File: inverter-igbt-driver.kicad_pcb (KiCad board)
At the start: 2 copper layers, 84.5 x 64 mm, 68 parts, among them J1 Conn_01x09, U1 NE555, U2 IXDF604SIA, U3 FOD8316, U5 FOD8316, U6 Transformer_2P_2S, U8 Transformer_2P_2S, U9 IGBT_HALF_BRIDGE

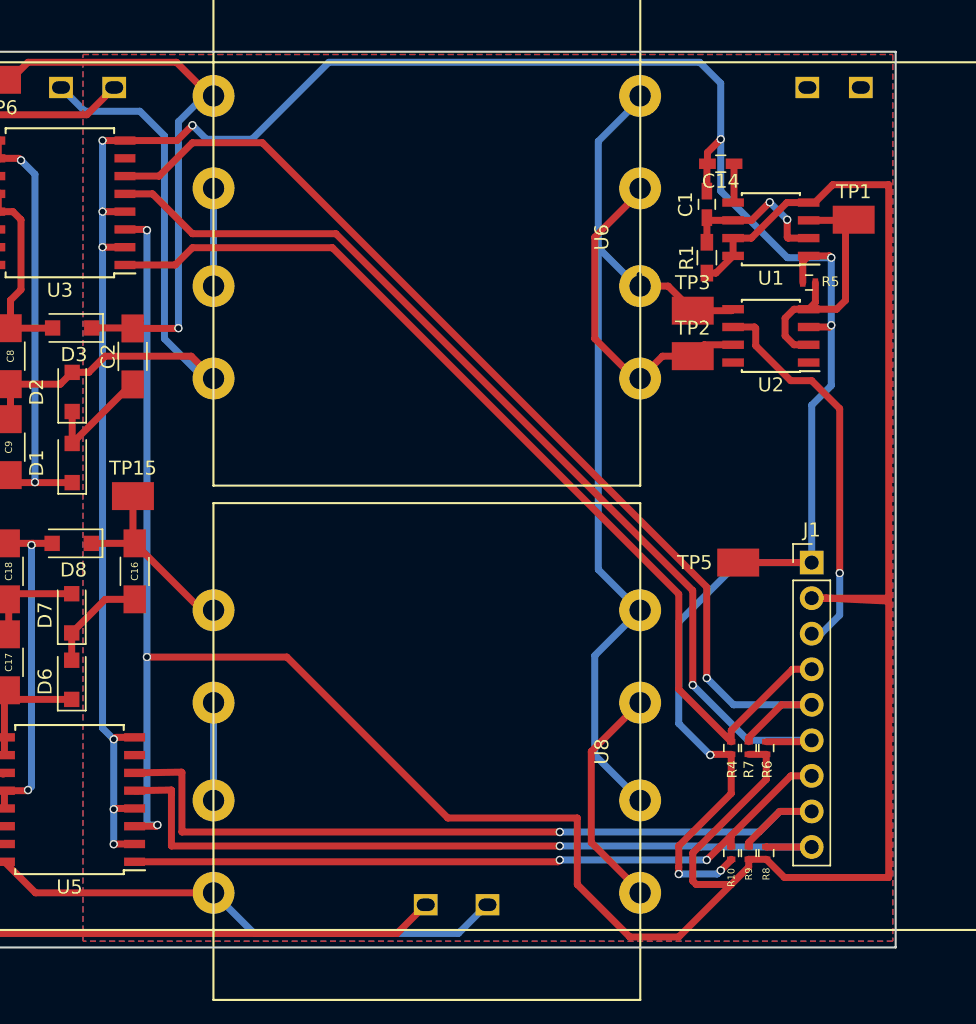
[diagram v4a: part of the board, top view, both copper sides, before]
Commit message: Adds NTC to connector.
Completes 555 rewire.

Rewires IGBT signals to layout more simply.
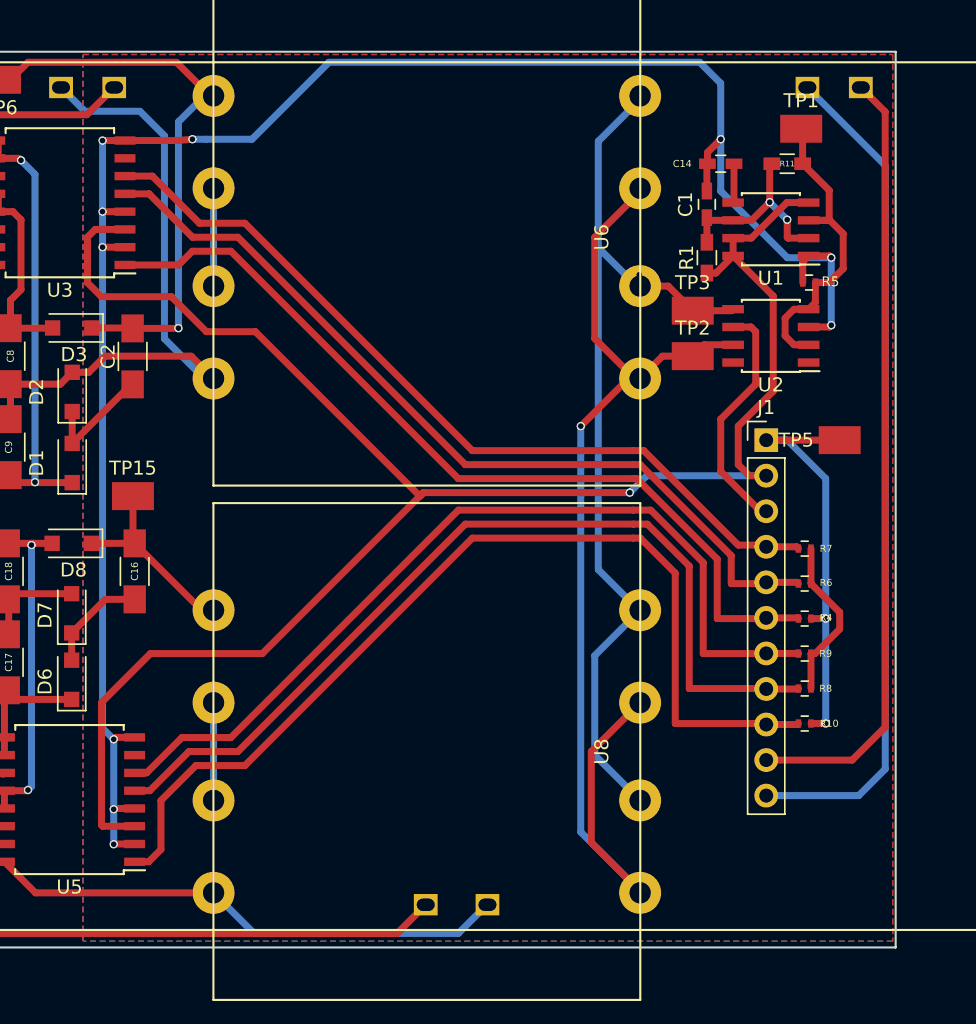
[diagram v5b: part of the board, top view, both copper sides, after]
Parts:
- added R11: 1.5k, Resistors_SMD:R_0603_HandSoldering, F.Cu at (169.8, 29.0)
- J1: value Conn_01x09 -> CONTROL; footprint Pin_Headers:Pin_Header_Straight_1x09_Pitch2.54mm -> Pin_Headers:Pin_Header_Straight_1x11_Pitch2.54mm
- moved R7 14.8 mm to (171.0, 56.5), turned to 180 degrees
- moved R9 14.8 mm to (171.0, 64.0), turned to 180 degrees
- moved R6 12.1 mm to (171.0, 59.0), turned to 180 degrees
- moved R8 12.1 mm to (171.0, 66.5), turned to 180 degrees
- moved TP5 11.4 mm to (173.5, 48.8)
- moved R10 10.6 mm to (171.0, 69.0), turned to 0 degrees
- moved R4 10.6 mm to (171.0, 61.5), turned to 0 degrees
- moved J1 9.33 mm to (168.2, 48.8)
- moved TP1 7.50 mm to (170.8, 26.5)
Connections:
- J1 pad 4: /VIN_H -> /FAULT_H
- J1 pad 5: /FAULT_H -> /RESET_H
- J1 pad 6: /RESET_H -> /VIN_H
- J1 pad 7: /VIN_L -> /FAULT_L
- J1 pad 8: /FAULT_L -> /RESET_L
- J1 pad 9: /RESET_L -> /VIN_L
- U9 pad 5: Net-(U9-Pad5) -> /NTC+
- U9 pad 6: Net-(U9-Pad6) -> /NTC-
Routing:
- net +5V: track 205.7 -> 143.8 mm, vias 3 -> 1
- net /NTC-: track 0.00 -> 60.3 mm
- net /NTC+: track 0.00 -> 55.9 mm
- net /negative/SQUARE_H: track 40.5 -> 81.2 mm, vias 0 -> 1
- net GND: track 198.6 -> 167.6 mm, vias 13 -> 12
- net /VIN_L: track 51.7 -> 70.9 mm, vias 2 -> 0
- net /FAULT_H: track 76.3 -> 59.1 mm, vias 1 -> 0
- net /RESET_H: track 72.5 -> 60.9 mm, vias 1 -> 0
- net +24V: track 28.1 -> 17.2 mm, vias 1 -> 0
- net /RESET_L: track 55.7 -> 65.3 mm, vias 1 -> 0
- net /VIN_H: track 70.8 -> 61.9 mm
- net Net-(R11-Pad1): track 18.1 -> 23.8 mm
- net /FAULT_L: track 59.0 -> 63.3 mm, vias 1 -> 0
- net Net-(C1-Pad1): track 11.4 -> 14.3 mm

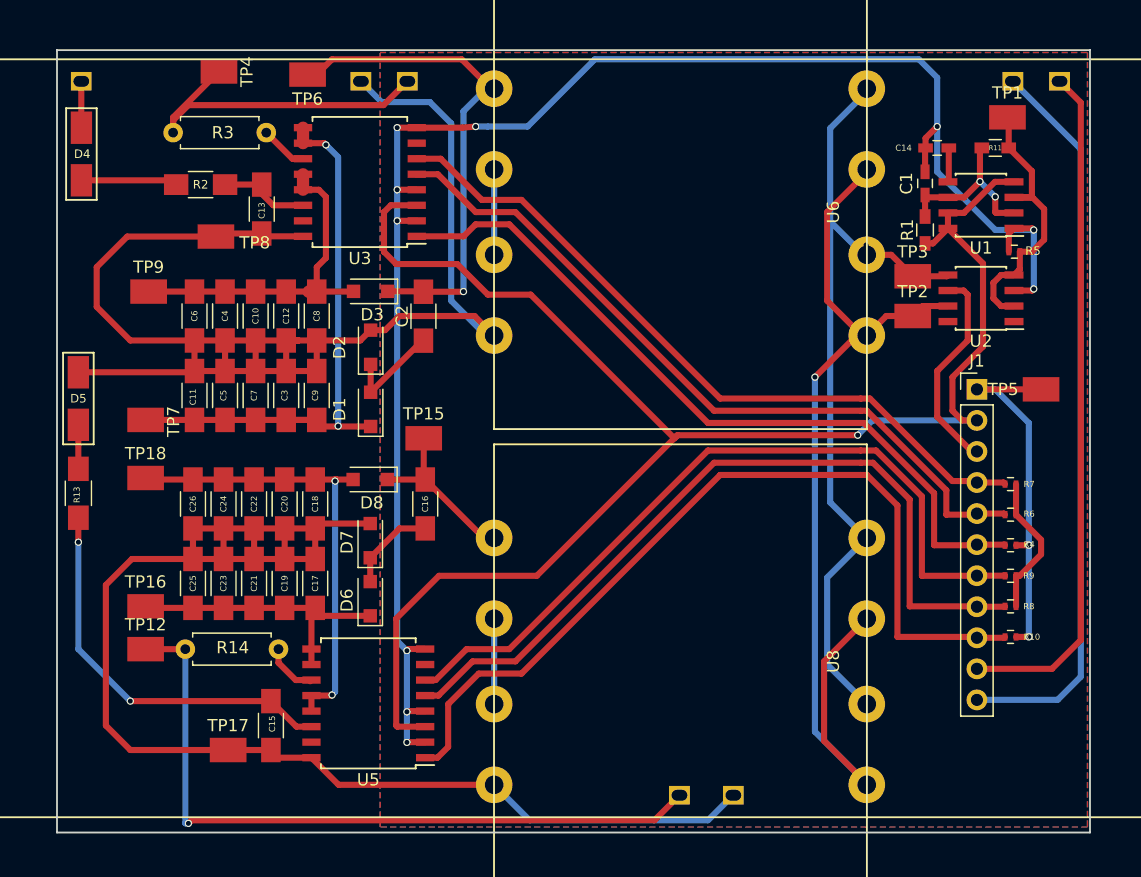
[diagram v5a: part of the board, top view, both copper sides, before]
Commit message: Fix hole size for avoiding slotting in OshPark drilling.
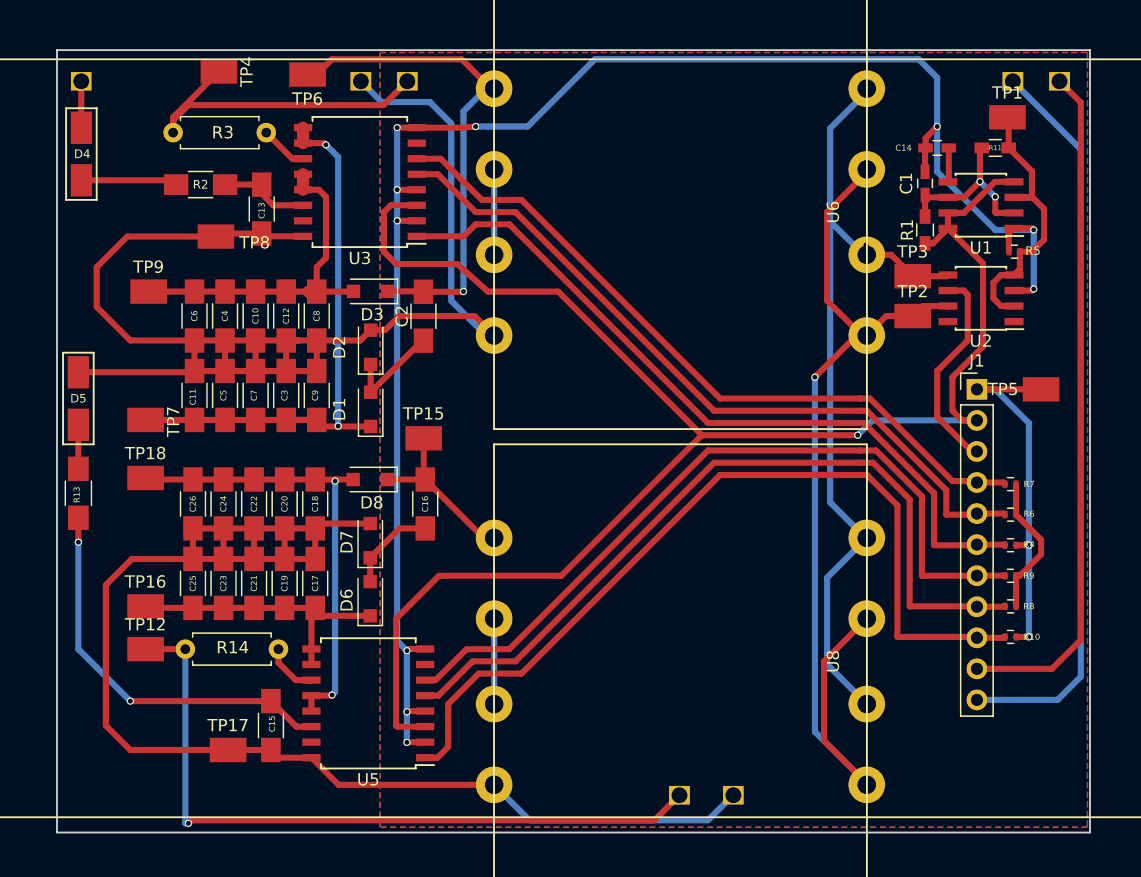
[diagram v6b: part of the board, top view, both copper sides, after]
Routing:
- net +5V: track 143.8 -> 145.6 mm
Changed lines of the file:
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@@
       (net 20 "Net-(C16-Pad2)"))
-  )
-  (module inverter-igbt-driver:MG06600WB-BN4MM (layer F.Cu)
-    (at 142.75 52.75)
-    (fp_text reference U9 (at 0 -29) (layer F.SilkS) hide
-      (effects (font (size 1 1) (thickness 0.15)))
-    )
-    (fp_text value IGBT_HALF_BRIDGE (at 0 -33) (layer F.Fab) hide
-      (effects (font (size 1 1) (thickness 0.15)))
-    )
-    (fp_line (start -61 0) (end -61 2) (layer F.SilkS) (width 0.15))
-    (fp_line (start -61 2) (end -76 2) (layer F.SilkS) (width 0.15))
-    (fp_line (start -76 2) (end -76 19.5) (layer F.SilkS) (width 0.15))
-    (fp_line (start -76 19.5) (end -61 19.5) (layer F.SilkS) (width 0.15))
-    (fp_line (start -61 19.5) (end -61 31) (layer F.SilkS) (width 0.15))
-    (fp_line (start -61 31) (end 61 31) (layer F.SilkS) (width 0.15))
-    (fp_line (start 61 31) (end 61 19.5) (layer F.SilkS) (width 0.15))
-    (fp_line (start 61 19.5) (end 76 19.5) (layer F.SilkS) (width 0.15))
-    (fp_line (start 76 19.5) (end 76 2) (layer F.SilkS) (width 0.15))
-    (fp_line (start 76 2) (end 61 2) (layer F.SilkS) (width 0.15))
-    (fp_line (start 61 2) (end 61 -2) (layer F.SilkS) (width 0.15))
-    (fp_line (start 61 -2) (end 76 -2) (layer F.SilkS) (width 0.15))
-    (fp_line (start 76 -2) (end 76 -19.5) (layer F.SilkS) (width 0.15))
-    (fp_line (start 76 -19.5) (end 61 -19.5) (layer F.SilkS) (width 0.15))
-    (fp_line (start 61 -19.5) (end 61 -31) (layer F.SilkS) (width 0.15))
-    (fp_line (start 61 -31) (end -61 -31) (layer F.SilkS) (width 0.15))
-    (fp_line (start -61 -31) (end -61 -19.5) (layer F.SilkS) (width 0.15))
-    (fp_line (start -61 -19.5) (end -76 -19.5) (layer F.SilkS) (width 0.15))
-    (fp_line (start -76 -19.5) (end -76 -2) (layer F.SilkS) (width 0.15))
-    (fp_line (start -76 -2) (end -61 -2) (layer F.SilkS) (width 0.15))
-    (fp_line (start -61 -2) (end -61 0) (layer F.SilkS) (width 0.15))
-    (pad 1 thru_hole rect (at 1.17 29.2) (size 1.7 1.524) (drill oval 1.3 0.9) (layers *.Cu *.Mask)
-      (net 28 /GATE_L))
-    (pad 2 thru_hole rect (at 5.58 29.2) (size 1.7 1.524) (drill oval 1.3 0.9) (layers *.Cu *.Mask)
-      (net 17 /EMIT_L))
-    (pad 5 thru_hole rect (at 32.26 -29.2) (size 1.7 1.524) (drill oval 1.3 0.9) (layers *.Cu *.Mask)
-      (net 42 /NTC+))
-    (pad 6 thru_hole rect (at 28.44 -29.2) (size 1.7 1.524) (drill oval 1.3 0.9) (layers *.Cu *.Mask)
-      (net 43 /NTC-))
-    (pad 7 thru_hole rect (at -21.09 -29.2) (size 1.7 1.524) (drill oval 1.3 0.9) (layers *.Cu *.Mask)
-      (net 37 /GATE_H))
-    (pad 8 thru_hole rect (at -24.89 -29.2) (size 1.7 1.524) (drill oval 1.3 0.9) (layers *.Cu *.Mask)
-      (net 23 /COLL_L))
-    (pad 9 thru_hole rect (at -47.76 -29.2) (size 1.7 1.524) (drill oval 1.3 0.9) (layers *.Cu *.Mask)
-      (net 36 /COLL_H))
   )
   (module Capacitors_SMD:C_0603_HandSoldering (layer F.Cu)
@@
       (rotate (xyz 0 0 0))
     )
+  )
+  (module inverter-igbt-driver:MG06600WB-BN4MM (layer F.Cu)
+    (at 142.75 52.75)
+    (fp_text reference U9 (at 0 -29) (layer F.SilkS) hide
+      (effects (font (size 1 1) (thickness 0.15)))
+    )
+    (fp_text value IGBT_HALF_BRIDGE (at 0 -33) (layer F.Fab) hide
+      (effects (font (size 1 1) (thickness 0.15)))
+    )
+    (fp_line (start -61 0) (end -61 2) (layer F.SilkS) (width 0.15))
+    (fp_line (start -61 2) (end -76 2) (layer F.SilkS) (width 0.15))
+    (fp_line (start -76 2) (end -76 19.5) (layer F.SilkS) (width 0.15))
+    (fp_line (start -76 19.5) (end -61 19.5) (layer F.SilkS) (width 0.15))
+    (fp_line (start -61 19.5) (end -61 31) (layer F.SilkS) (width 0.15))
+    (fp_line (start -61 31) (end 61 31) (layer F.SilkS) (width 0.15))
+    (fp_line (start 61 31) (end 61 19.5) (layer F.SilkS) (width 0.15))
+    (fp_line (start 61 19.5) (end 76 19.5) (layer F.SilkS) (width 0.15))
+    (fp_line (start 76 19.5) (end 76 2) (layer F.SilkS) (width 0.15))
+    (fp_line (start 76 2) (end 61 2) (layer F.SilkS) (width 0.15))
+    (fp_line (start 61 2) (end 61 -2) (layer F.SilkS) (width 0.15))
+    (fp_line (start 61 -2) (end 76 -2) (layer F.SilkS) (width 0.15))
+    (fp_line (start 76 -2) (end 76 -19.5) (layer F.SilkS) (width 0.15))
+    (fp_line (start 76 -19.5) (end 61 -19.5) (layer F.SilkS) (width 0.15))
+    (fp_line (start 61 -19.5) (end 61 -31) (layer F.SilkS) (width 0.15))
+    (fp_line (start 61 -31) (end -61 -31) (layer F.SilkS) (width 0.15))
+    (fp_line (start -61 -31) (end -61 -19.5) (layer F.SilkS) (width 0.15))
+    (fp_line (start -61 -19.5) (end -76 -19.5) (layer F.SilkS) (width 0.15))
+    (fp_line (start -76 -19.5) (end -76 -2) (layer F.SilkS) (width 0.15))
+    (fp_line (start -76 -2) (end -61 -2) (layer F.SilkS) (width 0.15))
+    (fp_line (start -61 -2) (end -61 0) (layer F.SilkS) (width 0.15))
+    (pad 1 thru_hole rect (at 1.17 29.2) (size 1.7 1.524) (drill 1.3) (layers *.Cu *.Mask)
+      (net 28 /GATE_L))
+    (pad 2 thru_hole rect (at 5.58 29.2) (size 1.7 1.524) (drill 1.3) (layers *.Cu *.Mask)
+      (net 17 /EMIT_L))
+    (pad 5 thru_hole rect (at 32.26 -29.2) (size 1.7 1.524) (drill 1.3) (layers *.Cu *.Mask)
+      (net 42 /NTC+))
+    (pad 6 thru_hole rect (at 28.44 -29.2) (size 1.7 1.524) (drill 1.3) (layers *.Cu *.Mask)
+      (net 43 /NTC-))
+    (pad 7 thru_hole rect (at -21.09 -29.2) (size 1.7 1.524) (drill 1.3) (layers *.Cu *.Mask)
+      (net 37 /GATE_H))
+    (pad 8 thru_hole rect (at -24.89 -29.2) (size 1.7 1.524) (drill 1.3) (layers *.Cu *.Mask)
+      (net 23 /COLL_L))
+    (pad 9 thru_hole rect (at -47.76 -29.2) (size 1.7 1.524) (drill 1.3) (layers *.Cu *.Mask)
+      (net 36 /COLL_H))
   )
   (gr_line (start 93 85) (end 93 21) (angle 90) (layer Edge.Cuts) (width 0.15))
@@
   (segment (start 95 31.65) (end 102.4 31.65) (width 0.5) (layer F.Cu) (net 6))
   (segment (start 102.4 31.65) (end 102.75 32) (width 0.5) (layer F.Cu) (net 6))
-  (segment (start 143.75 52.5) (end 158.5 52.5) (width 0.5) (layer F.Cu) (net 7))
-  (segment (start 159.71 51.29) (end 168.25 51.29) (width 0.5) (layer B.Cu) (net 7) (status 800000))
+  (segment (start 145.75 52.5) (end 158.5 52.5) (width 0.5) (layer F.Cu) (net 7))
+  (segment (start 159.71 51.29) (end 168.25 51.29) (width 0.5) (layer B.Cu) (net 7))
   (segment (start 158.5 52.5) (end 159.71 51.29) (width 0.5) (layer B.Cu) (net 7))
   (via (at 158.5 52.5) (size 0.6) (drill 0.4) (layers F.Cu B.Cu) (net 7))
-  (segment (start 122.428 33.693) (end 120.307 33.693) (width 0.5) (layer F.Cu) (net 7) (status 400000))
+  (segment (start 122.428 33.693) (end 120.307 33.693) (width 0.5) (layer F.Cu) (net 7))
   (segment (start 120.838 76.338) (end 120.75 76.25) (width 0.5) (layer F.Cu) (net 7))
   (segment (start 120.75 76.25) (end 120.75 67.5) (width 0.5) (layer F.Cu) (net 7))
   (segment (start 120.75 67.5) (end 124.25 64) (width 0.5) (layer F.Cu) (net 7))
-  (segment (start 124.25 64) (end 132.25 64) (width 0.5) (layer F.Cu) (net 7))
-  (segment (start 132.25 64) (end 143.75 52.5) (width 0.5) (layer F.Cu) (net 7))
-  (segment (start 143.75 52.5) (end 143.5 52.75) (width 0.5) (layer F.Cu) (net 7))
-  (segment (start 120.838 76.338) (end 123.1165 76.338) (width 0.5) (layer F.Cu) (net 7) (status 800000))
-  (segment (start 131.75 41) (end 143.5 52.75) (width 0.5) (layer F.Cu) (net 7))
-  (segment (start 128.25 41) (end 131.75 41) (width 0.5) (layer F.Cu) (net 7))
-  (segment (start 125.75 38.5) (end 128.25 41) (width 0.5) (layer F.Cu) (net 7))
+  (segment (start 124.25 64) (end 134.25 64) (width 0.5) (layer F.Cu) (net 7))
+  (segment (start 134.25 64) (end 145.75 52.5) (width 0.5) (layer F.Cu) (net 7))
+  (segment (start 145.75 52.5) (end 145.75 52.5) (width 0.5) (layer F.Cu) (net 7))
+  (segment (start 120.838 76.338) (end 123.1165 76.338) (width 0.5) (layer F.Cu) (net 7))
+  (segment (start 134 40.75) (end 145.75 52.5) (width 0.5) (layer F.Cu) (net 7))
+  (segment (start 128.25 40.75) (end 134 40.75) (width 0.5) (layer F.Cu) (net 7))
+  (segment (start 125.75 38.5) (end 128.25 40.75) (width 0.5) (layer F.Cu) (net 7))
   (segment (start 120.75 38.5) (end 125.75 38.5) (width 0.5) (layer F.Cu) (net 7))
   (segment (start 119.75 37.5) (end 120.75 38.5) (width 0.5) (layer F.Cu) (net 7))

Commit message: Changing 555 timer again to remove pullup resistor and discharge.
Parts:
- removed R1: 100k, Resistors_SMD:R_0603_HandSoldering
- moved R11 6.02 mm to (174.2, 33.0), turned to 90 degrees
- moved TP1 2.24 mm to (171.8, 28.5)
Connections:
- R11 pad 1: Net-(R11-Pad1) -> Net-(C1-Pad1)
- R11 pad 2: Net-(C1-Pad1) -> Net-(R11-Pad2)
- R5 pad 1: Net-(R11-Pad1) -> Net-(R11-Pad2)
- TP1 pad 1: Net-(R11-Pad1) -> Net-(R11-Pad2)
- U1 pad 3: Net-(R11-Pad1) -> Net-(R11-Pad2)
- U1 pad 7: +5V -> Net-(U1-Pad7)
- U2 pad 2: Net-(R11-Pad1) -> Net-(R11-Pad2)
- U2 pad 4: Net-(R11-Pad1) -> Net-(R11-Pad2)
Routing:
- net Net-(R11-Pad2): track 0.00 -> 24.5 mm
- net Net-(R11-Pad1): track 23.8 -> 0.00 mm
- net +5V: track 145.6 -> 149.1 mm
- net Net-(C1-Pad1): track 14.3 -> 12.0 mm
